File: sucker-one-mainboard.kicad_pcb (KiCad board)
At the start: 4 copper layers, 68 x 67.3 mm, 112 parts, among them J1 JST NC Valve, J10 BM10B-SRSS-TB(LF)(SN), J11 UART/SWD DNP, J12 TYPE-C-31-M-12, J2 JST NO Valve, J3 6P4C, J4 JST 3 Way Valve, J5 Jack-DC, J6 Phoenix Contact 1733570, J7 QWIIC I2C, J8 SPI, J9 BM04B-SRSS-TBT(LF)(SN), Q1 BSS138, Q2 BSS138, Q3 BSS138, SW1 BOOTSEL, U1 LD1117S33TR, U2 TPS62143RGTT, U3 W25Q128JVPIQ TR, U4 RP2040, Y1 ABMM2-12.000MHZ-E2-T

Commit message: WiP Layout Ref 2
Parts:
- added Q4: STN4NF20L, STN4NF20L:SOT223, F.Cu at (76.3, 133.2)
- moved R20 95.2 mm to (78.1, 130.2), turned to -90 degrees
- moved C5 89.6 mm to (79.6, 130.2), turned to -90 degrees
- moved D5 88.4 mm to (70.7, 131.1), turned to 180 degrees
- moved R19 79.7 mm to (75.2, 130.8), turned to 180 degrees
- moved D4 69.0 mm to (92.2, 148.8), turned to -90 degrees
- moved R13 57.3 mm to (105.4, 131.6), turned to 180 degrees
- moved F1 57.3 mm to (74.9, 150.0), turned to 180 degrees
- moved C21 54.9 mm to (106.0, 150.2), turned to -90 degrees
- moved R23 50.9 mm to (124.4, 150.2), turned to 90 degrees
- moved R24 43.5 mm to (126.2, 150.2), turned to 90 degrees
- moved J9 36.7 mm to (109.6, 137.3)
- moved D1 32.4 mm to (117.5, 140.9), turned to 90 degrees
- moved C24 31.1 mm to (127.8, 133.3), turned to 180 degrees
- moved J10 27.4 mm to (122.0, 134.9)
- moved C25 20.0 mm to (126.0, 132.3), turned to 180 degrees
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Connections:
- D1 pad 1: FOOTPEDAL_AUX -> FPATVS
- D1 pad 2: FOOTPEDAL -> FPTVS
- J3 pad 2: Net-(J3-Pad2) -> FPTVS
- J3 pad 3: Net-(J3-Pad3) -> FPATVS
- R23 pad 1: Net-(J3-Pad3) -> FPATVS
- R24 pad 1: Net-(J3-Pad2) -> FPTVS
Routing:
- net BEMF: track 0.00 -> 49.4 mm, vias 0 -> 4
- net (no net): track 32.2 -> 0.00 mm, vias 5 -> 0
- net Net-(C5-Pad1): track 58.7 -> 89.1 mm, vias 0 -> 2
- net +5V: track 108.0 -> 131.8 mm, vias 8 -> 18
- net Net-(J5-Pad2): track 0.00 -> 23.2 mm
- net FPTVS: track 0.00 -> 21.4 mm, vias 0 -> 2
- net FPATVS: track 0.00 -> 19.1 mm
- net UI LED Data: track 25.4 -> 8.46 mm, vias 2 -> 0
- net MOTOR_PWM: track 27.9 -> 12.0 mm
- net Net-(J10-Pad9): track 0.00 -> 15.3 mm, vias 0 -> 2
- net Net-(F1-Pad2): track 0.00 -> 14.2 mm, vias 0 -> 1
- net +12V: track 136.4 -> 150.4 mm, vias 2 -> 1
- net Net-(C5-Pad2): track 0.00 -> 14.0 mm, vias 0 -> 2
- net +3V3: track 47.5 -> 55.8 mm, vias 21 -> 20
- net Low Btn: track 26.5 -> 32.7 mm
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- added copper zone on F.Cu, net +5V
- added copper zone on In2.Cu, net +5V
- added copper zone on F.Cu, net GND

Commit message: Finished Ref 2 layout
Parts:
- added kibuzzard-6107E0E1: G***, kibuzzard-6107E0E1, F.Cu at (122.1, 139.5)
- added kibuzzard-6107E29B: G***, kibuzzard-6107E29B, F.Cu at (121.2, 126.7)
- added kibuzzard-6107E2CE: G***, kibuzzard-6107E2CE, F.Cu at (109.8, 126.3)
- added kibuzzard-6107E302: G***, kibuzzard-6107E302, F.Cu at (109.6, 134.0)
- added kibuzzard-6107E44E: G***, kibuzzard-6107E44E, F.Cu at (94.5, 118.7)
- added kibuzzard-6107E45C: G***, kibuzzard-6107E45C, F.Cu at (94.5, 110.6)
- added kibuzzard-6107E4A2: G***, kibuzzard-6107E4A2, F.Cu at (106.4, 116.9)
- added kibuzzard-61080AF0: G***, kibuzzard-61080AF0, F.Cu at (77.5, 111.3)
- added kibuzzard-61080B06: G***, kibuzzard-61080B06, F.Cu at (75.6, 113.8)
- added kibuzzard-61080B37: G***, kibuzzard-61080B37, F.Cu at (82.7, 113.8)
- moved TP28 42.2 mm to (109.2, 126.0)
- moved C27 41.8 mm to (111.3, 124.7), turned to 90 degrees
- moved TP27 40.7 mm to (107.7, 128.0)
- moved TP25 38.7 mm to (110.1, 128.4)
- moved J7 35.4 mm to (124.5, 126.7)
- moved TP15 34.7 mm to (123.4, 127.8)
- moved TP26 33.6 mm to (106.8, 122.2)
- moved R22 33.4 mm to (121.2, 120.7), turned to -90 degrees
- moved TP14 32.8 mm to (121.8, 121.8)
- moved R21 32.2 mm to (119.4, 120.7), turned to -90 degrees
- moved C26 25.2 mm to (123.3, 131.8)
- moved J8 25.0 mm to (106.4, 126.3), turned to -90 degrees
- moved D7 23.8 mm to (115.3, 129.3)
- moved D2 21.9 mm to (115.3, 122.4), turned to -90 degrees
- moved R10 21.3 mm to (113.5, 129.3), turned to -90 degrees
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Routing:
- net Net-(D7-Pad1): track 42.6 -> 74.5 mm, vias 3 -> 9
- net Net-(D2-Pad1): track 53.0 -> 77.3 mm, vias 5 -> 8
- net I2C0_SDA: track 37.2 -> 57.2 mm, vias 3 -> 8
- net I2C0_SCL: track 36.7 -> 56.3 mm, vias 3 -> 7
- net SPI0_CLK: track 55.0 -> 37.2 mm, vias 5 -> 1
- net SPI0_MISO: track 59.0 -> 42.3 mm, vias 5 -> 4
- net SPI0_MOSI: track 59.0 -> 44.2 mm, vias 5 -> 2
- net +3V3: track 55.8 -> 68.3 mm, vias 20 -> 21
- net +12V: track 150.4 -> 162.0 mm, vias 1 -> 2
- net SPI0_CS: track 54.4 -> 44.4 mm, vias 6 -> 7
- net Net-(C5-Pad1): track 89.1 -> 94.5 mm
- net +5V: track 131.8 -> 137.2 mm
- net NO_VALVE: track 79.9 -> 85.1 mm, vias 8 -> 6
- net Net-(D10-Pad2): track 54.0 -> 57.9 mm, vias 8 -> 6
- net Net-(R26-Pad2): track 46.5 -> 50.2 mm, vias 2 -> 4
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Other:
- board text added: "3W"
- board text added: "NC"
- board text added: "NO"
- board text added: "by Robin Reiter Hergatz, DE Aug 2021"

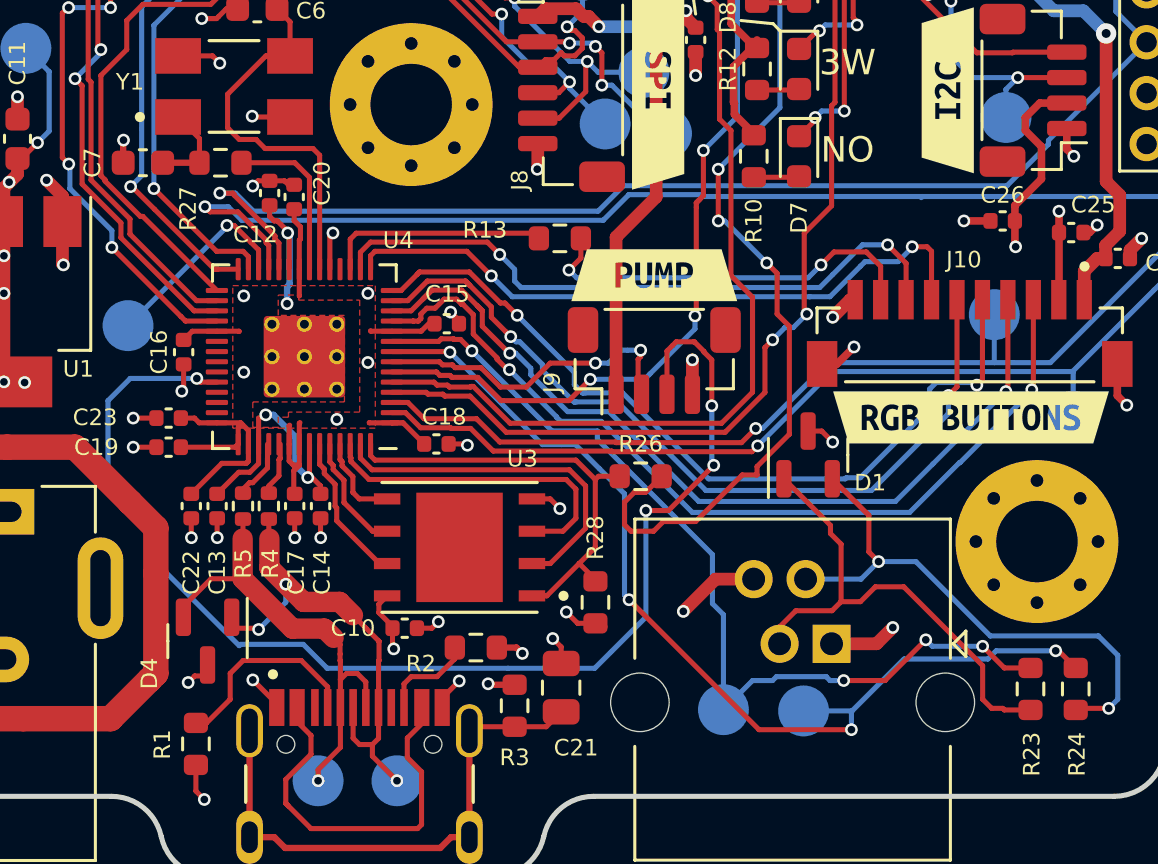
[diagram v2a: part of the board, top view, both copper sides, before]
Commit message: Update passives around RP2040
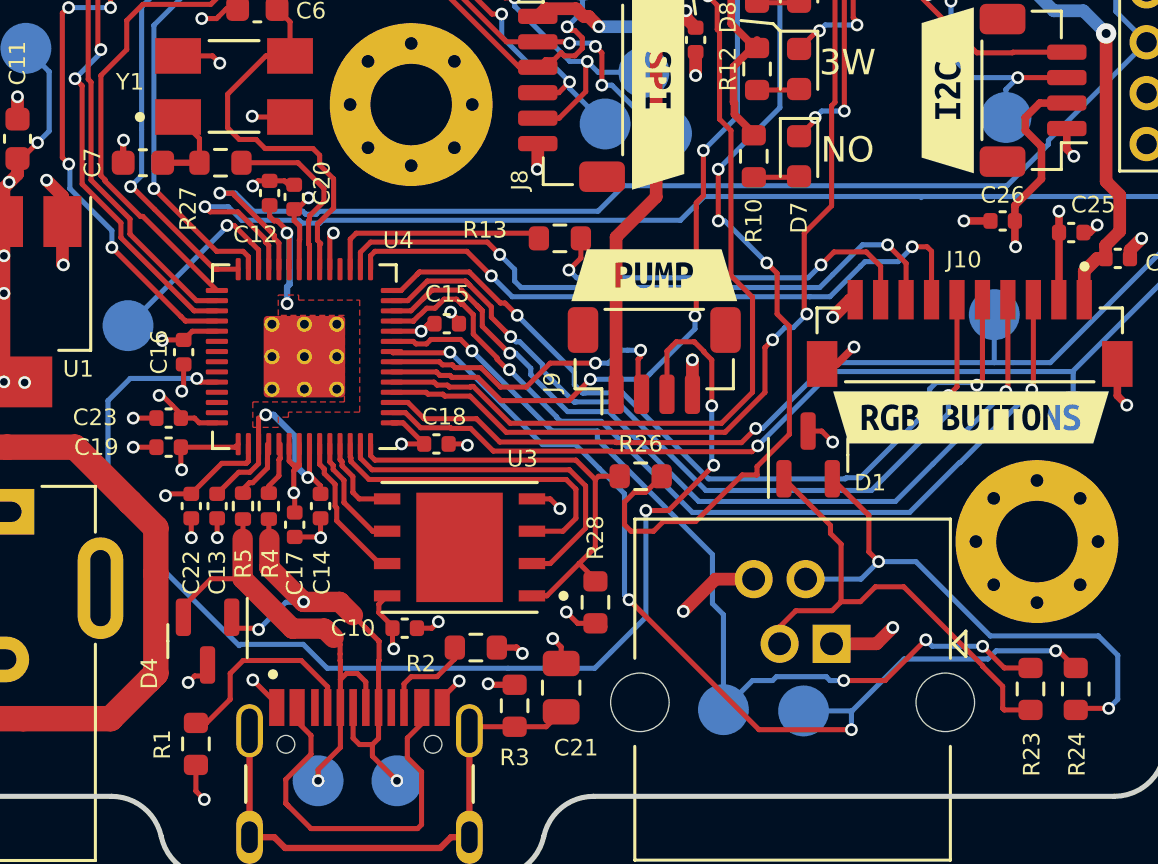
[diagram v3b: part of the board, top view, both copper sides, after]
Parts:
- moved C17 0.73 mm to (95.5, 143.8)
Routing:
- net GND: track 90.8 -> 61.5 mm, vias 69 -> 68
- net +3V3: track 68.3 -> 67.3 mm, vias 21 -> 24
- net OSC_OUT: track 6.52 -> 7.09 mm
- net OSC_IN: track 15.0 -> 15.6 mm
- removed copper zone on F.Cu, net +3V3

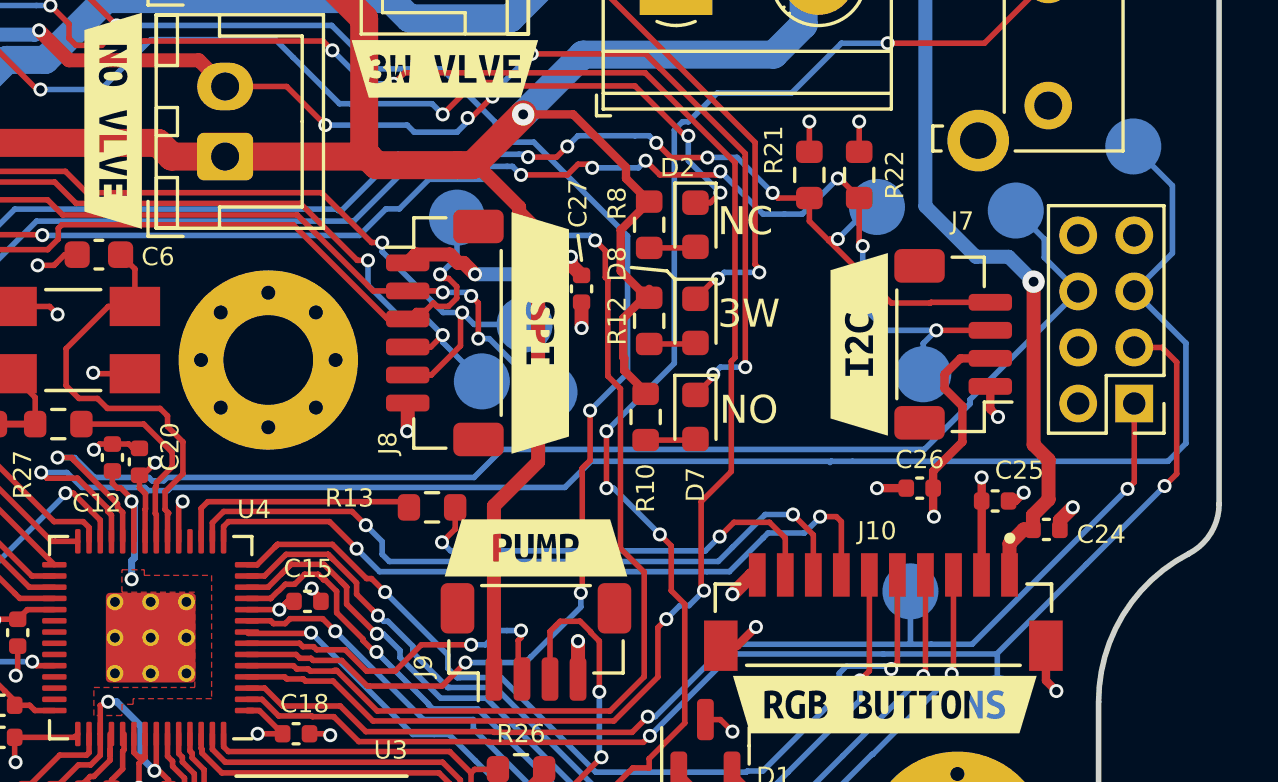
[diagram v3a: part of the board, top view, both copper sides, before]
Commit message: Add UI board level shifting
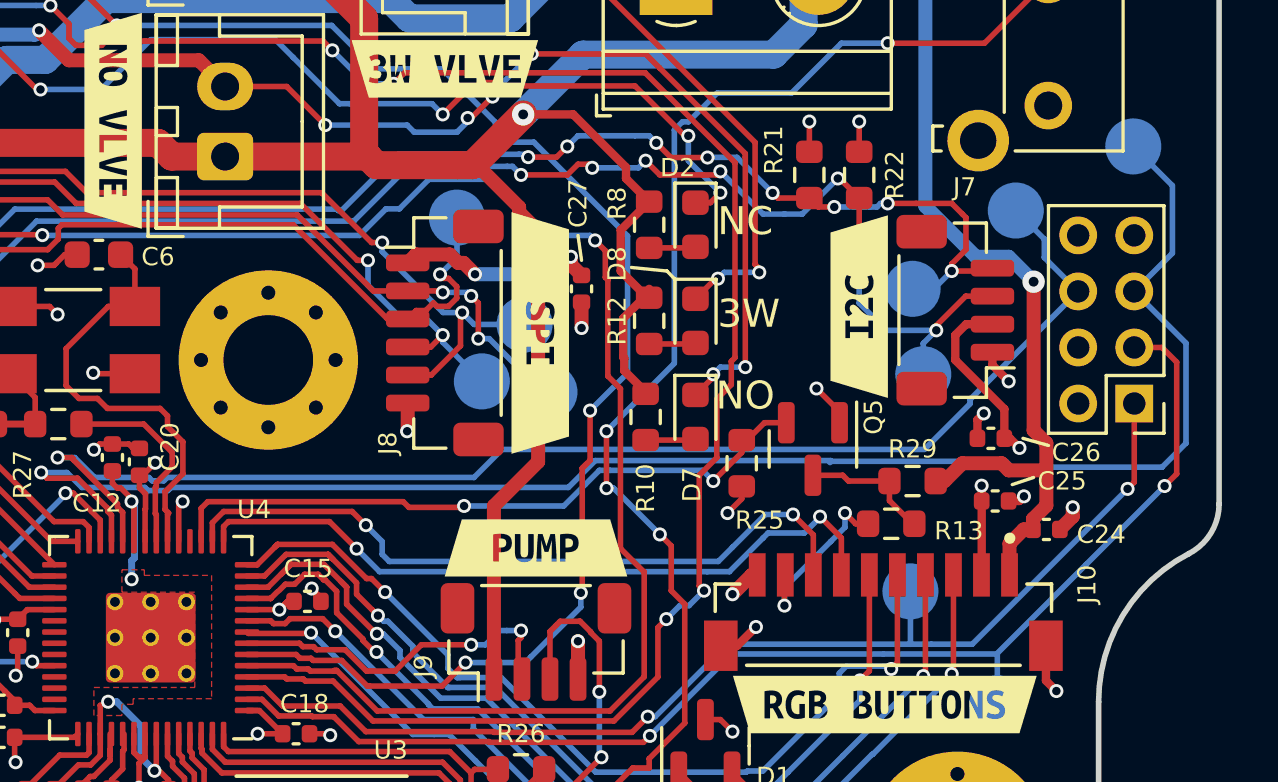
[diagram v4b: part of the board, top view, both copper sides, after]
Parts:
- added Q5: BSS138, Package_TO_SOT_SMD:SOT-23, F.Cu at (119.5, 130.4)
- added R25: 10k, Resistor_SMD:R_0603_1608Metric, F.Cu at (117.0, 130.9)
- added R29: 10k, Resistor_SMD:R_0603_1608Metric, F.Cu at (123.1, 131.6)
- moved R13 16.4 mm to (122.3, 133.1), turned to 0 degrees
- moved TP14 3.19 mm to (123.1, 124.7)
- moved C26 3.10 mm to (125.9, 130.0)
- moved kibuzzard-6107E29B 1.35 mm to (121.2, 125.3)
- moved J7 1.22 mm to (124.6, 125.5)
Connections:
- R13 pad 2: UI LED Data -> LED_DATA
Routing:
- net UI LED Data: track 8.77 -> 24.1 mm, vias 0 -> 2
- net Net-(J10-Pad9): track 15.8 -> 6.29 mm
- net LED_DATA: track 0.00 -> 4.74 mm
- net +5V: track 137.2 -> 141.4 mm
- net +3V3: track 67.3 -> 68.7 mm, vias 24 -> 26
- net I2C0_SDA: track 57.2 -> 57.9 mm
- net I2C0_SCL: track 56.3 -> 56.8 mm, vias 7 -> 9

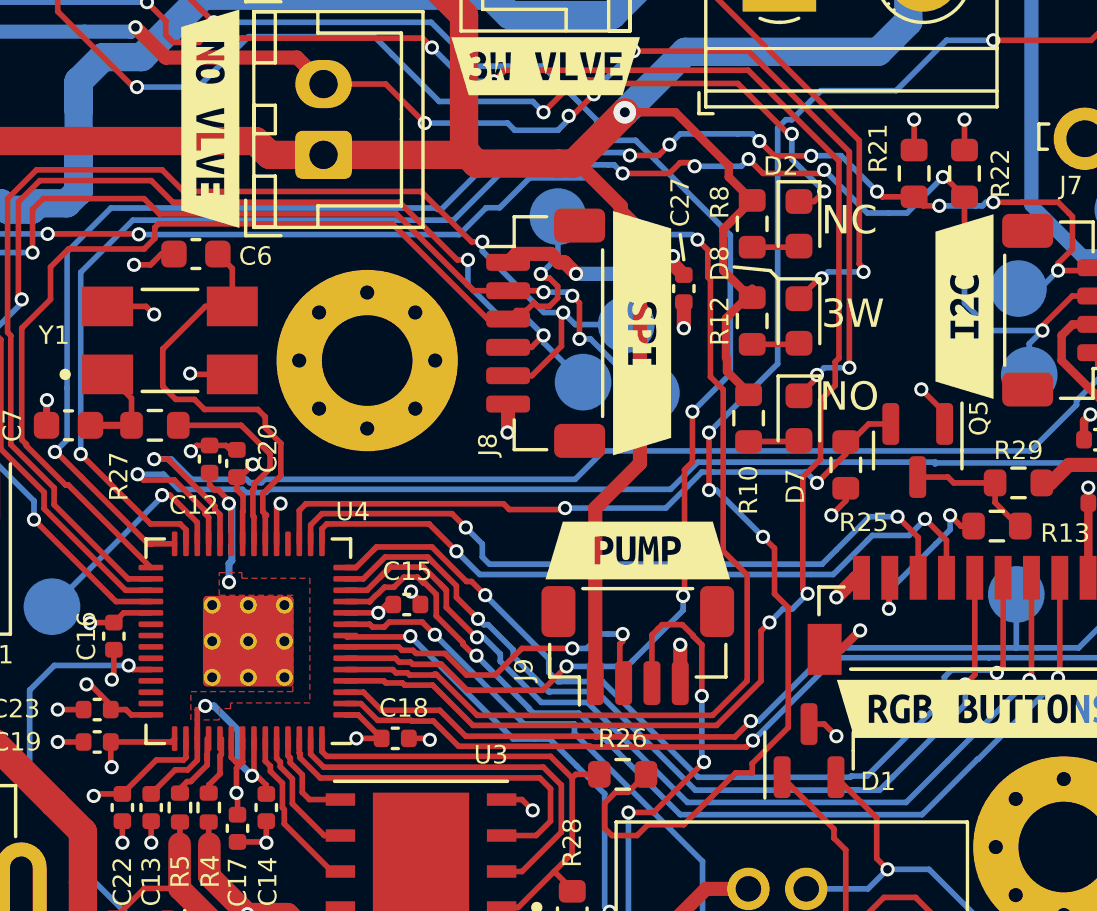
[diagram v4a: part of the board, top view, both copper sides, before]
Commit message: Updated pad below RP2040
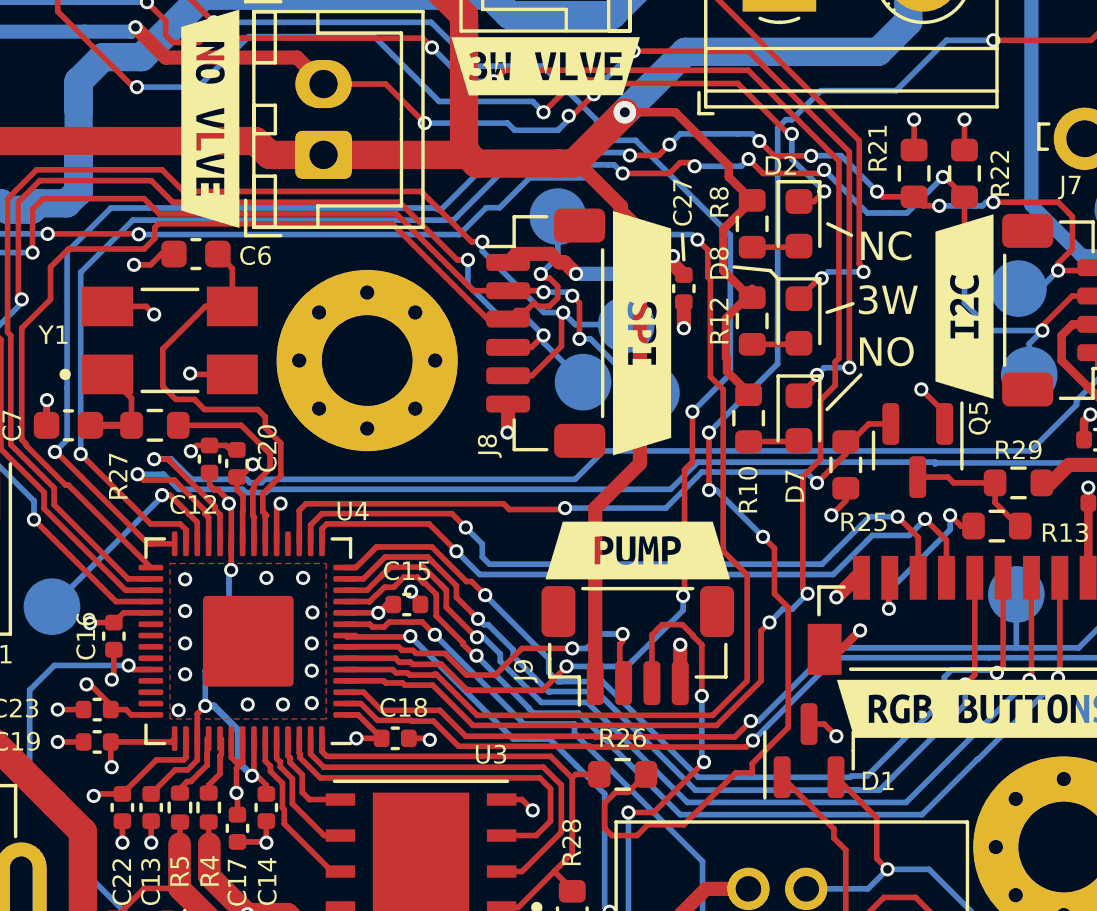
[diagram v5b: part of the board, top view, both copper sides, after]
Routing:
- net +1V1: track 15.3 -> 18.9 mm
- net GND: vias 68 -> 81
- removed copper zone on F.Cu, net +1V1
